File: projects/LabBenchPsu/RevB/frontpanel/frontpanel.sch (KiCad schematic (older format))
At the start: 52 parts, among them CON1 USB-A-stacked, CON2 USB-A-stacked, CON3 USB-A-stacked, K1 TERMINAL, P1 INPUT_TERMINAL, P10 BindingPost, P11 LoadSwitch, P12 CONN_2, P13 BindingPost, P14 BindingPost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

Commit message: working on schematic and footprints
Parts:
- P10, P13, P14, P15, P8: footprint (none) -> frep:BindingPost
- P11: footprint (none) -> frep:LoadSwitch
- P16: footprint (none) -> frep:JST-PH-2-THM
- P9: footprint (none) -> frep:RockerSwitch
- R1, R18, R2, R4, R5, R6, R7: footprint (none) -> frep:R0805
- R3: footprint (none) -> frep:R_ceramic_48x9p5x9mm
- U1, U2, U3: footprint (none) -> frep:SOT23-6
- U4: footprint (none) -> frep:SOT223
- U6, U7: footprint (none) -> frep:MSOP10
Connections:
- net ADJ: now reaches K1.1 (P1), P10.1
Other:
- note added: "Binding posts"
- note added: "Input / Output"
- note added: "LiPo charging 1s"
- note added: "Load Resistor"
- note added: "MCU"
- note added: "On/Off switch"
- note added: "Power indicator"
- note added: "Screw PSU cables here!"
- note added: "TPS2513 optional for\nfaster charging"
- note added: "Terminal connector"
- note added: "USB charging"
- note added: "connectors"
- note added: "dpst"
- note added: "external voltage"
- note added: "i2c"
- note added: "load switch"
- note added: "o"
- note added: "power regulation"
- note added: "screw-\nterminal\n(power)"
- note added: "serial"
- note removed: "Load Resistor\n(if necessary)"
- note removed: "Terminal connector\nScrew PSU cables here!"
- note removed: "i2c connector"
- note removed: "load switch (dpst)"
- note removed: "screwterminal\n(power)"
- note removed: "serial connector"
- note removed: "terminals (incl fuses)"
- moved on the sheet: C1, C2, C3, C4, C5, C6, C7, CON1, CON2, CON3, D1, D2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

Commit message: start with pcb
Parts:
- U5: footprint (none) -> frep:featherEsp
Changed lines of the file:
@@
 F 0 "U5" H 10275 1175 40  0000 C CNN
 F 1 "esp8266Feather" H 10275 2500 40  0000 C CNN
-F 2 "" H 10275 2025 40  0001 C CNN
+F 2 "frep:featherEsp" H 10275 2025 40  0001 C CNN
 F 3 "" H 10275 2025 40  0000 C CNN
 	1    10275 1800

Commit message: pcb in progress
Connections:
- net 3V3Reg: now also P12.1 (P1)
- net 5V: no longer P12.1 (P1)
- net GND: now also R18.2; no longer D3.2 (K)
- net at D3.1 (A): now also P12.2 (PM); no longer R18.2
- net loadOn: now reaches R18.1
- net loadOn: now also D3.2 (K); no longer P12.2 (PM)
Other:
- moved on the sheet: D3, R18
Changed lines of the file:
@@
 L LED D3
 U 1 1 5752944F
-P 5775 2100
-F 0 "D3" H 5775 2200 50  0000 C CNN
-F 1 "LoadOn" H 5775 1975 50  0000 C CNN
-F 2 "frep:LED-0805" H 5775 2100 60  0001 C CNN
-F 3 "" H 5775 2100 60  0000 C CNN
-	1    5775 2100
+P 5775 1600
+F 0 "D3" H 5775 1700 50  0000 C CNN
+F 1 "LoadOn" H 5775 1475 50  0000 C CNN
+F 2 "frep:LED-0805" H 5775 1600 60  0001 C CNN
+F 3 "" H 5775 1600 60  0000 C CNN
+	1    5775 1600
 	0    1    1    0
 $EndComp
@@
 L R R18
 U 1 1 57529455
-P 5775 1650
-F 0 "R18" V 5855 1650 40  0000 C CNN
-F 1 "1K" V 5782 1651 40  0000 C CNN
-F 2 "frep:R0805" V 5705 1650 30  0001 C CNN
-F 3 "" H 5775 1650 30  0000 C CNN
-	1    5775 1650
+P 5775 2050
+F 0 "R18" V 5855 2050 40  0000 C CNN
+F 1 "1K" V 5782 2051 40  0000 C CNN
+F 2 "frep:R0805" V 5705 2050 30  0001 C CNN
+F 3 "" H 5775 2050 30  0000 C CNN
+	1    5775 2050
 	1    0    0    -1
 $EndComp
@@
 	1    0    0    -1
 $EndComp
-Text GLabel 5775 1200 1    40   Input ~ 0
-5V
 $Comp
 L CONN_3 K1
@@
 Wire Notes Line
 	5650 4675 5650 2850
+Text GLabel 5775 1800 2    40   Input ~ 0
+loadOn
+Text GLabel 5775 1200 1    40   Input ~ 0
+3V3Reg
 $EndSCHEMATC

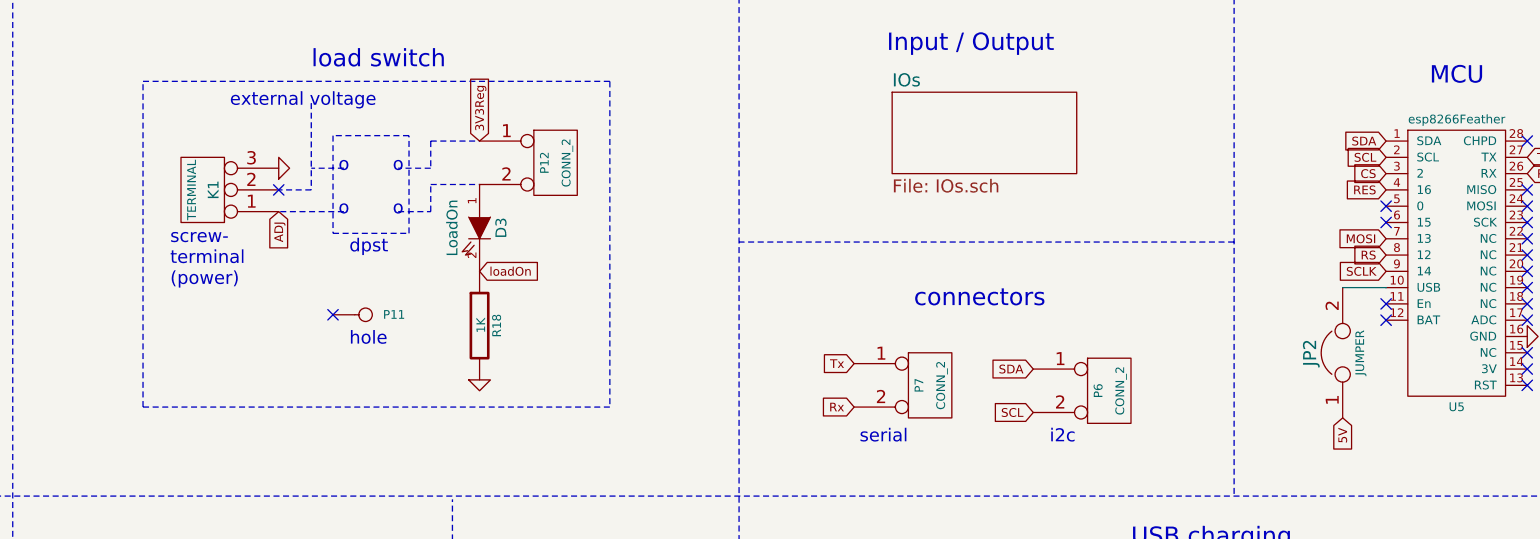
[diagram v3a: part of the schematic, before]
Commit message: protective diodes added
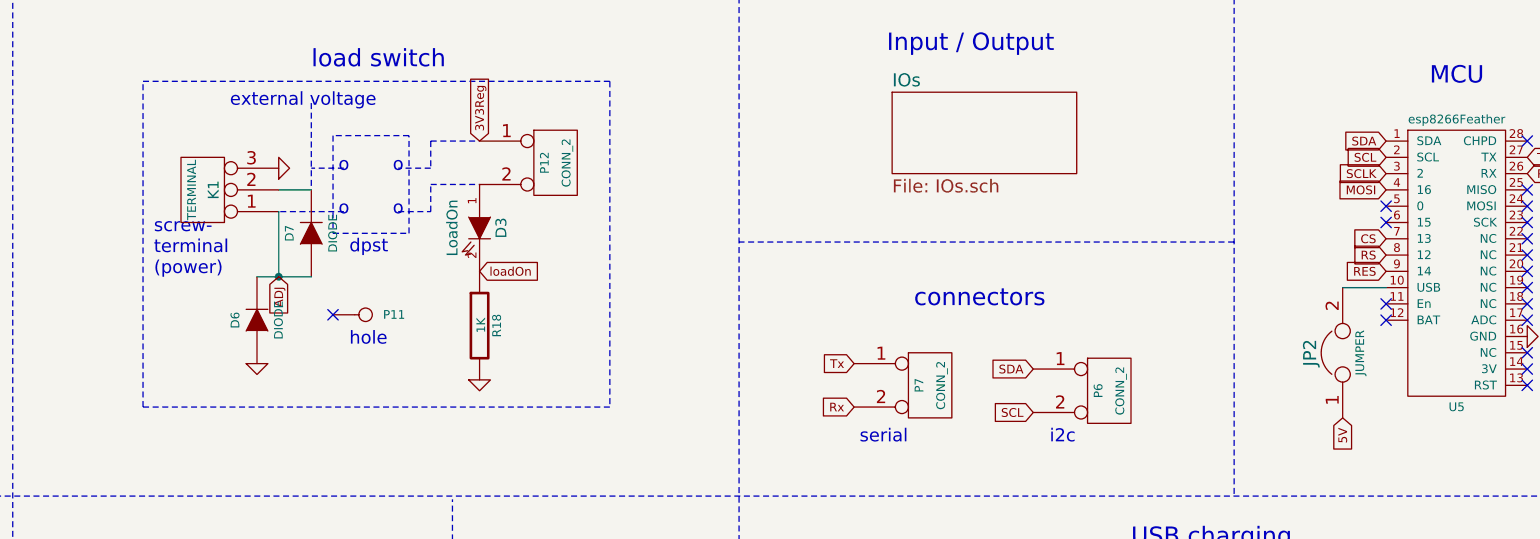
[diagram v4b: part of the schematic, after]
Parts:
- added D6, D7: DIODE, frep:DO-221BC, symbol DIODE
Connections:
- net ADJ: now also D6.2 (K), D7.1 (A)
- net CS: now also U5.7 (13); no longer U5.3 (2)
- net GND: now also D6.1 (A)
- net MOSI: now also U5.4 (16); no longer U5.7 (13)
- net RES: now also U5.9 (14); no longer U5.4 (16)
- net SCLK: now also U5.3 (2); no longer U5.9 (14)
- net at K1.2 (PM): now also D7.2 (K)
- no-connect marks 25 -> 24
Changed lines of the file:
@@
 NoConn ~ 6100 7350
 NoConn ~ 6100 7500
+Text GLabel 9950 1425 0    40   Input ~ 0
+MOSI
 Text GLabel 9950 1650 0    40   Input ~ 0
-MOSI
-Text GLabel 9950 1350 0    40   Input ~ 0
 CS
 Text GLabel 9950 1725 0    40   Input ~ 0
 RS
+Text GLabel 9950 1350 0    40   Input ~ 0
+SCLK
 Text GLabel 9950 1800 0    40   Input ~ 0
-SCLK
-Text GLabel 9950 1425 0    40   Input ~ 0
 RES
 NoConn ~ 10600 2025
@@
 	-1   0    0    1
 $EndComp
-Text Notes 4350 1875 0    60   ~ 0
+Text Notes 4275 1825 0    60   ~ 0
 screw-\nterminal\n(power)
 Text Notes 5175 2150 0    60   ~ 0
@@
 	1    0    0    -1
 $EndComp
-NoConn ~ 4850 1425
 Text GLabel 6150 5225 2    40   Input ~ 0
 12V
@@
 Text GLabel 5425 4050 1    40   Input ~ 0
 ADJ
-Text GLabel 4850 1525 3    40   Input ~ 0
+Text GLabel 4850 1825 3    40   Input ~ 0
 ADJ
 Text Notes 2200 2175 0    60   ~ 0
@@
 	5550 1400 5775 1400
 Wire Notes Line
-	5150 1525 4850 1525
-Wire Notes Line
 	5150 1325 5000 1325
 Wire Notes Line
 	5000 1025 5000 1425
-Wire Notes Line
-	5000 1425 4850 1425
 Wire Notes Line
 	700  1150 700  2250
@@
 Text GLabel 5775 1200 1    40   Input ~ 0
 3V3Reg
+$Comp
+L DIODE D6
+U 1 1 578FDAEA
+P 4750 2025
+F 0 "D6" H 4750 2125 40  0000 C CNN
+F 1 "DIODE" H 4750 1925 40  0000 C CNN
+F 2 "frep:DO-221BC" H 4750 2025 60  0001 C CNN
+F 3 "" H 4750 2025 60  0000 C CNN
+	1    4750 2025
+	0    -1   -1   0
+$EndComp
+$Comp
+L DIODE D7
+U 1 1 578FDBA4
+P 5000 1625
+F 0 "D7" H 5000 1725 40  0000 C CNN
+F 1 "DIODE" H 5000 1525 40  0000 C CNN
+F 2 "frep:DO-221BC" H 5000 1625 60  0001 C CNN
+F 3 "" H 5000 1625 60  0000 C CNN
+	1    5000 1625
+	0    -1   -1   0
+$EndComp
+$Comp
+L GND #PWR050
+U 1 1 578FE713
+P 4750 2225
+F 0 "#PWR050" H 4750 2225 30  0001 C CNN
+F 1 "GND" H 4750 2155 30  0001 C CNN
+F 2 "" H 4750 2225 60  0000 C CNN
+F 3 "" H 4750 2225 60  0000 C CNN
+	1    4750 2225
+	1    0    0    -1
+$EndComp
+Wire Wire Line
+	5000 1425 4850 1425
+Wire Wire Line
+	4850 1825 4850 1525
+Wire Wire Line
+	4750 1825 5000 1825
+Connection ~ 4850 1825
+Wire Notes Line
+	5150 1525 4850 1525
 $EndSCHEMATC
